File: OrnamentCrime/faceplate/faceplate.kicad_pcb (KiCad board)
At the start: 2 copper layers, 70.8 x 128.4 mm, 24 parts, among them J1 Conn_01x01_Female, J3 Conn_01x01_Female, J4 Conn_01x01_Female, J5 Conn_01x01_Female, J6 Conn_01x01_Female

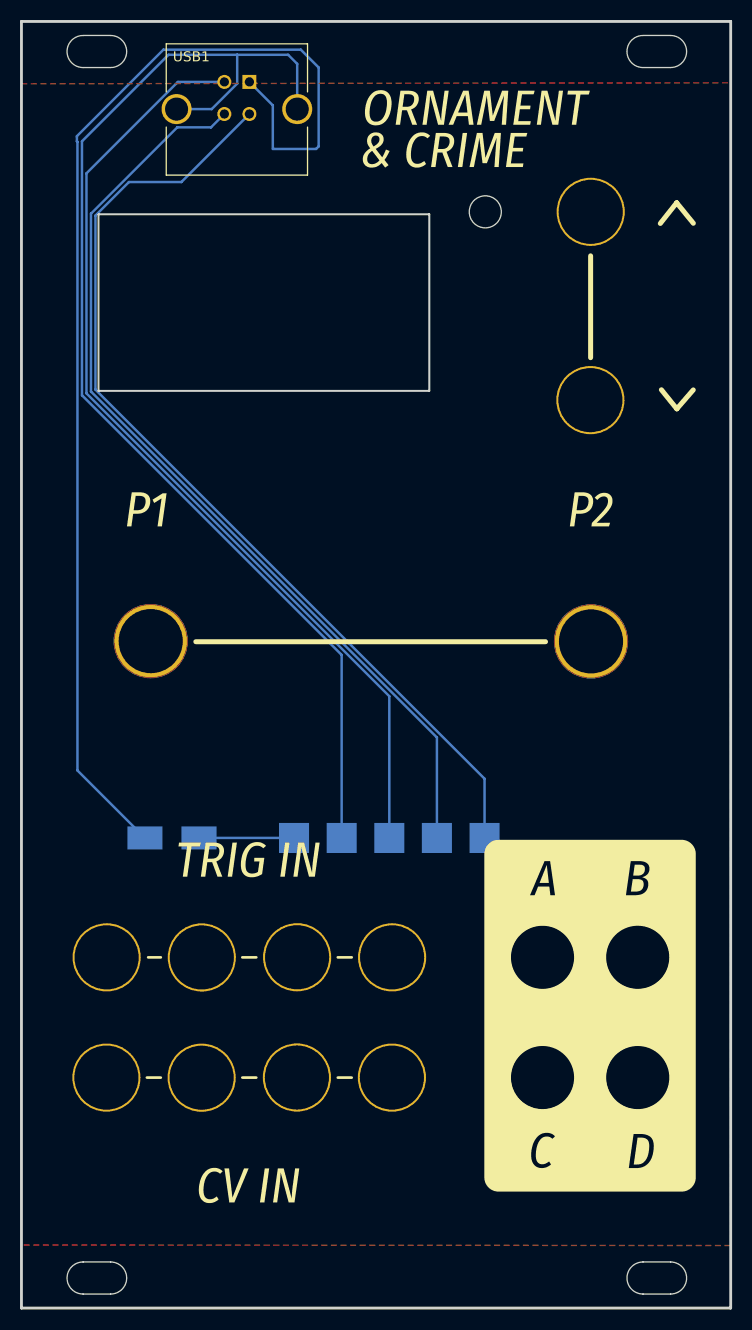
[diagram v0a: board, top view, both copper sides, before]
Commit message: Thicken power traces for USB connector
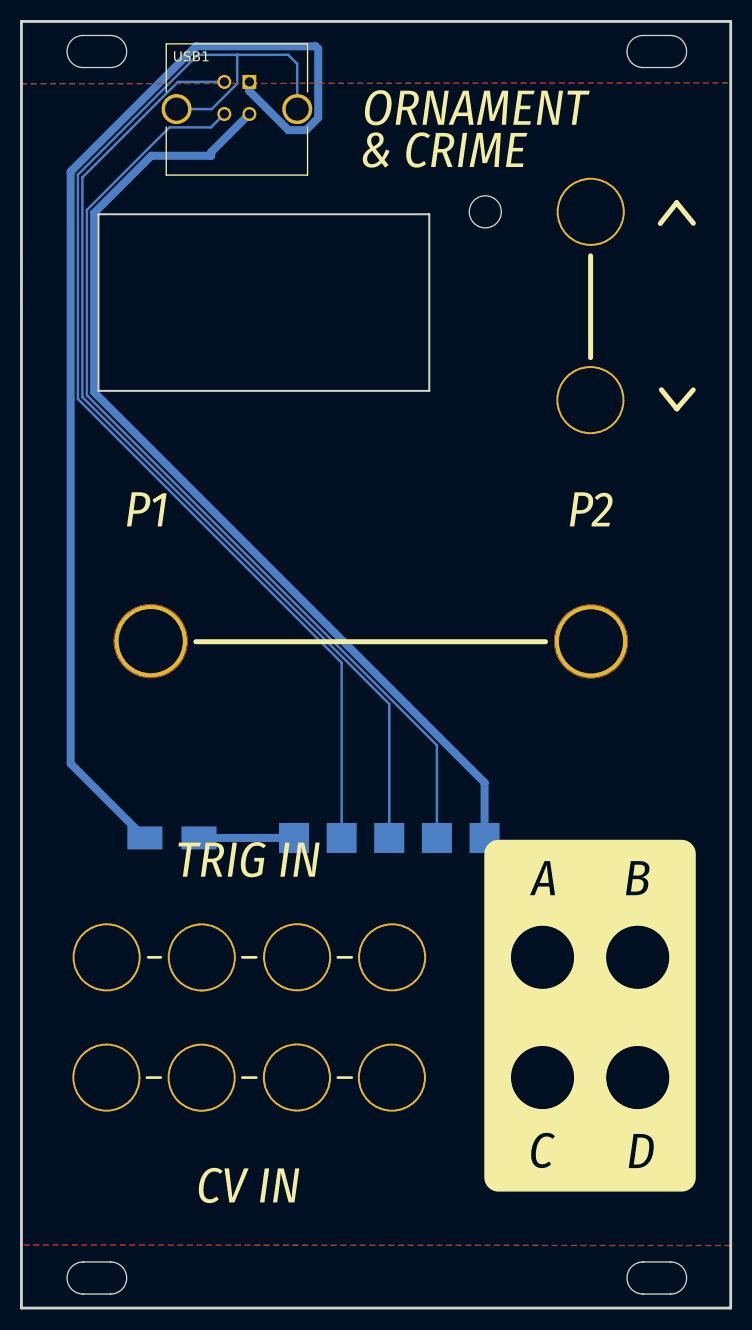
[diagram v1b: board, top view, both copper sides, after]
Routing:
- net Net-(D1-Pad2): track 121.5 -> 116.3 mm
- net /SHIELD: track 120.2 -> 118.8 mm
- net /D+: track 94.0 -> 94.8 mm
- net /GND: track 97.8 -> 98.3 mm
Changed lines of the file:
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@@
   )
   (setup
+    (stackup
+      (layer "F.SilkS" (type "Top Silk Screen"))
+      (layer "F.Paste" (type "Top Solder Paste"))
+      (layer "F.Mask" (type "Top Solder Mask") (thickness 0.01))
+      (layer "F.Cu" (type "copper") (thickness 0.035))
+      (layer "dielectric 1" (type "core") (thickness 1.51) (material "FR4") (epsilon_r 4.5) (loss_tangent 0.02))
+      (layer "B.Cu" (type "copper") (thickness 0.035))
+      (layer "B.Mask" (type "Bottom Solder Mask") (thickness 0.01))
+      (layer "B.Paste" (type "Bottom Solder Paste"))
+      (layer "B.SilkS" (type "Bottom Silk Screen"))
+      (copper_finish "None")
+      (dielectric_constraints no)
+    )
     (pad_to_mask_clearance 0)
+    (grid_origin 85.8 32.935)
     (pcbplotparams
       (layerselection 0x00010fc_ffffffff)
@@
     (effects (font (size 1 1) (thickness 0.15)) (justify mirror))
   )
-  (segment (start 90.932 29.718) (end 92.71 31.496) (width 0.25) (layer "B.Cu") (net 1))
-  (segment (start 92.71 31.496) (end 92.71 39.37) (width 0.25) (layer "B.Cu") (net 1))
-  (segment (start 92.456 39.624) (end 88.138 39.624) (width 0.25) (layer "B.Cu") (net 1))
-  (segment (start 68.638 38.92) (end 68.58 38.862) (width 0.25) (layer "B.Cu") (net 1))
-  (segment (start 88.138 39.624) (end 88.138 35.273) (width 0.25) (layer "B.Cu") (net 1))
-  (segment (start 68.58 38.862) (end 68.58 38.354) (width 0.25) (layer "B.Cu") (net 1))
-  (segment (start 75.37 108.38) (end 68.638 101.648) (width 0.25) (layer "B.Cu") (net 1))
-  (segment (start 92.71 39.37) (end 92.456 39.624) (width 0.25) (layer "B.Cu") (net 1))
-  (segment (start 68.58 38.354) (end 77.216 29.718) (width 0.25) (layer "B.Cu") (net 1))
-  (segment (start 88.138 35.273) (end 85.8 32.935) (width 0.25) (layer "B.Cu") (net 1))
-  (segment (start 68.638 101.648) (end 68.638 38.92) (width 0.25) (layer "B.Cu") (net 1))
-  (segment (start 77.216 29.718) (end 90.932 29.718) (width 0.25) (layer "B.Cu") (net 1))
-  (segment (start 90.245 108.38) (end 90.252 108.387) (width 0.25) (layer "B.Cu") (net 2))
-  (segment (start 80.77 108.38) (end 90.245 108.38) (width 0.25) (layer "B.Cu") (net 2))
-  (segment (start 69.088 38.862) (end 77.724 30.226) (width 0.25) (layer "B.Cu") (net 3))
+  (segment (start 92.67 36.514142) (end 92.67 29.645) (width 0.8) (layer "B.Cu") (net 1))
+  (segment (start 91.439142 37.745) (end 92.67 36.514142) (width 0.8) (layer "B.Cu") (net 1))
+  (segment (start 85.8 33.844849) (end 89.700151 37.745) (width 0.8) (layer "B.Cu") (net 1))
+  (segment (start 89.700151 37.745) (end 91.439142 37.745) (width 0.8) (layer "B.Cu") (net 1))
+  (segment (start 67.957996 100.967996) (end 75.37 108.38) (width 0.8) (layer "B.Cu") (net 1))
+  (segment (start 92.67 29.645) (end 92.404 29.379) (width 0.8) (layer "B.Cu") (net 1))
+  (segment (start 85.8 32.935) (end 85.8 33.844849) (width 0.8) (layer "B.Cu") (net 1))
+  (segment (start 80.466 29.379) (end 67.957996 41.887004) (width 0.8) (layer "B.Cu") (net 1))
+  (segment (start 92.404 29.379) (end 80.466 29.379) (width 0.8) (layer "B.Cu") (net 1))
+  (segment (start 67.957996 41.887004) (end 67.957996 100.967996) (width 0.8) (layer "B.Cu") (net 1))
+  (segment (start 90.245 108.38) (end 90.252 108.387) (width 0.8) (layer "B.Cu") (net 2))
+  (segment (start 80.77 108.38) (end 90.245 108.38) (width 0.8) (layer "B.Cu") (net 2))
   (segment (start 89.662 30.226) (end 90.57 31.134) (width 0.25) (layer "B.Cu") (net 3))
   (segment (start 82.039569 35.645) (end 84.582 33.102569) (width 0.25) (layer "B.Cu") (net 3))
+  (segment (start 68.682497 42.187103) (end 80.6436 30.226) (width 0.25) (layer "B.Cu") (net 3))
+  (segment (start 80.6436 30.226) (end 84.582 30.226) (width 0.25) (layer "B.Cu") (net 3))
   (segment (start 78.53 35.645) (end 82.039569 35.645) (width 0.25) (layer "B.Cu") (net 3))
   (segment (start 90.57 31.134) (end 90.57 35.645) (width 0.25) (layer "B.Cu") (net 3))
-  (segment (start 69.088 64.202553) (end 69.088 38.862) (width 0.25) (layer "B.Cu") (net 3))
-  (segment (start 77.724 30.226) (end 84.582 30.226) (width 0.25) (layer "B.Cu") (net 3))
+  (segment (start 95.0055 90.897165) (end 68.682497 64.574161) (width 0.25) (layer "B.Cu") (net 3))
+  (segment (start 95.0055 108.387) (end 95.0055 90.897165) (width 0.25) (layer "B.Cu") (net 3))
   (segment (start 84.582 33.102569) (end 84.582 30.226) (width 0.25) (layer "B.Cu") (net 3))
-  (segment (start 95.0055 90.120053) (end 69.088 64.202553) (width 0.25) (layer "B.Cu") (net 3))
+  (segment (start 68.682497 64.574161) (end 68.682497 42.187103) (width 0.25) (layer "B.Cu") (net 3))
   (segment (start 84.582 30.226) (end 89.662 30.226) (width 0.25) (layer "B.Cu") (net 3))
-  (segment (start 95.0055 108.387) (end 95.0055 90.120053) (width 0.25) (layer "B.Cu") (net 3))
-  (segment (start 73.777223 42.926) (end 79.009 42.926) (width 0.25) (layer "B.Cu") (net 4))
-  (segment (start 79.009 42.926) (end 85.8 36.135) (width 0.25) (layer "B.Cu") (net 4))
-  (segment (start 70.436503 46.26672) (end 73.777223 42.926) (width 0.25) (layer "B.Cu") (net 4))
-  (segment (start 70.436503 63.64328) (end 70.436503 46.26672) (width 0.25) (layer "B.Cu") (net 4))
-  (segment (start 109.266 102.472777) (end 70.436503 63.64328) (width 0.25) (layer "B.Cu") (net 4))
-  (segment (start 109.266 108.387) (end 109.266 102.472777) (width 0.25) (layer "B.Cu") (net 4))
-  (segment (start 104.5125 108.387) (end 104.5125 98.355673) (width 0.25) (layer "B.Cu") (net 5))
-  (segment (start 78.597533 37.47) (end 81.965 37.47) (width 0.25) (layer "B.Cu") (net 5))
-  (segment (start 69.987002 46.080531) (end 78.597533 37.47) (width 0.25) (layer "B.Cu") (net 5))
-  (segment (start 104.5125 98.355673) (end 69.987002 63.830175) (width 0.25) (layer "B.Cu") (net 5))
+  (segment (start 70.306 46.008315) (end 76.013315 40.301) (width 0.8) (layer "B.Cu") (net 4))
+  (segment (start 109.266 102.861685) (end 70.306 63.901685) (width 0.8) (layer "B.Cu") (net 4))
+  (segment (start 70.306 63.901685) (end 70.306 46.008315) (width 0.8) (layer "B.Cu") (net 4))
+  (segment (start 109.266 108.387) (end 109.266 102.861685) (width 0.8) (layer "B.Cu") (net 4))
+  (segment (start 76.013315 40.301) (end 81.99 40.301) (width 0.8) (layer "B.Cu") (net 4))
+  (segment (start 81.99 39.945) (end 85.8 36.135) (width 0.8) (layer "B.Cu") (net 4))
+  (segment (start 81.99 40.301) (end 81.99 39.945) (width 0.8) (layer "B.Cu") (net 4))
+  (segment (start 69.581499 45.708216) (end 77.819715 37.47) (width 0.25) (layer "B.Cu") (net 5))
   (segment (start 81.965 37.47) (end 83.3 36.135) (width 0.25) (layer "B.Cu") (net 5))
-  (segment (start 69.987002 63.830175) (end 69.987002 46.080531) (width 0.25) (layer "B.Cu") (net 5))
+  (segment (start 69.581499 64.201783) (end 69.581499 45.708216) (width 0.25) (layer "B.Cu") (net 5))
+  (segment (start 77.819715 37.47) (end 81.965 37.47) (width 0.25) (layer "B.Cu") (net 5))
+  (segment (start 104.5125 108.387) (end 104.5125 99.132785) (width 0.25) (layer "B.Cu") (net 5))
+  (segment (start 104.5125 99.132785) (end 69.581499 64.201783) (width 0.25) (layer "B.Cu") (net 5))
+  (segment (start 69.131998 64.387972) (end 69.131998 42.462062) (width 0.25) (layer "B.Cu") (net 6))
+  (segment (start 99.759 108.387) (end 99.759 95.014975) (width 0.25) (layer "B.Cu") (net 6))
   (segment (start 78.65906 32.935) (end 83.3 32.935) (width 0.25) (layer "B.Cu") (net 6))
-  (segment (start 69.537501 42.056559) (end 78.65906 32.935) (width 0.25) (layer "B.Cu") (net 6))
-  (segment (start 99.759 94.237863) (end 69.537501 64.016364) (width 0.25) (layer "B.Cu") (net 6))
-  (segment (start 69.537501 64.016364) (end 69.537501 42.056559) (width 0.25) (layer "B.Cu") (net 6))
-  (segment (start 99.759 108.387) (end 99.759 94.237863) (width 0.25) (layer "B.Cu") (net 6))
+  (segment (start 99.759 95.014975) (end 69.131998 64.387972) (width 0.25) (layer "B.Cu") (net 6))
+  (segment (start 69.131998 42.462062) (end 78.65906 32.935) (width 0.25) (layer "B.Cu") (net 6))
   (zone (net 0) (net_name "") (layer "F.Cu") (hatch edge 0.508)
     (connect_pads (clearance 0.508))
